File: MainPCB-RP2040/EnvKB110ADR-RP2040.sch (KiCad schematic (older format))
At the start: 272 parts, among them J2 EVQPU, J5 Conn_01x03_Male, U1 TLV75533PDBVR, U3 RP2040, Y1 3225_4P

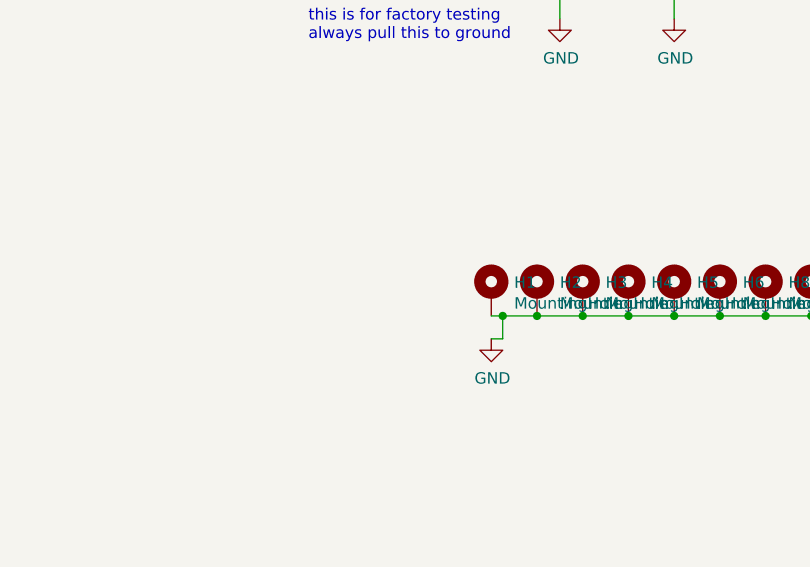
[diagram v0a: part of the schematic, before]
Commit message: added mount holes, fixed a couple trace errors, created backplate PCB
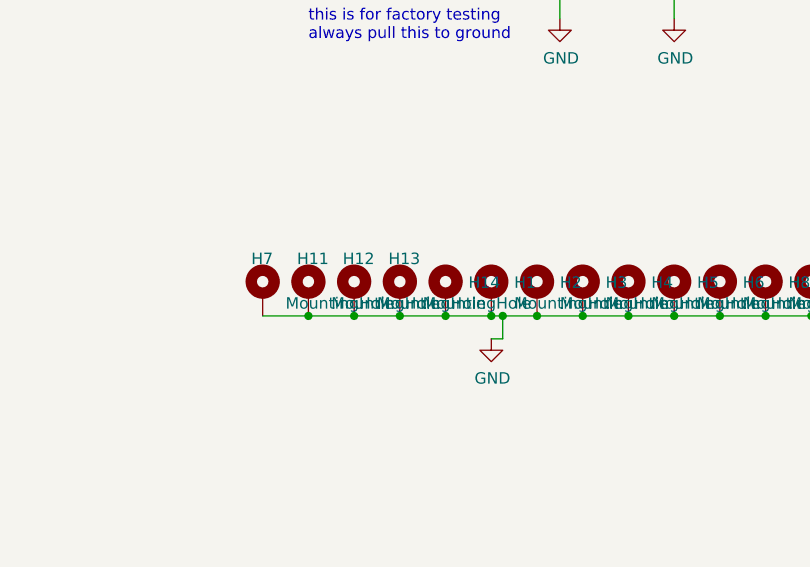
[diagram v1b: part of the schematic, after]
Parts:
- added H11, H12, H13, H14, H7: MountingHole, MountingHole:MountingHole_2.2mm_M2_Pad, symbol Mechanical:MountingHole_Pad
- H1, H10, H2, H3, H4, H5, H6, H8, H9: footprint MountingHole:MountingHole_2.2mm_M2 -> MountingHole:MountingHole_2.2mm_M2_Pad
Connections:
- net GND: now also H11.1, H12.1, H13.1, H14.1, H7.1
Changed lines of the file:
@@
 F 0 "H1" H 7100 9046 50  0000 L CNN
 F 1 "MountingHole" H 7100 8955 50  0000 L CNN
-F 2 "MountingHole:MountingHole_2.2mm_M2" H 7000 9000 50  0001 C CNN
+F 2 "MountingHole:MountingHole_2.2mm_M2_Pad" H 7000 9000 50  0001 C CNN
 F 3 "~" H 7000 9000 50  0001 C CNN
 	1    7000 9000
@@
 F 0 "H2" H 7300 9046 50  0000 L CNN
 F 1 "MountingHole" H 7300 8955 50  0000 L CNN
-F 2 "MountingHole:MountingHole_2.2mm_M2" H 7200 9000 50  0001 C CNN
+F 2 "MountingHole:MountingHole_2.2mm_M2_Pad" H 7200 9000 50  0001 C CNN
 F 3 "~" H 7200 9000 50  0001 C CNN
 	1    7200 9000
@@
 F 0 "H3" H 7500 9046 50  0000 L CNN
 F 1 "MountingHole" H 7500 8955 50  0000 L CNN
-F 2 "MountingHole:MountingHole_2.2mm_M2" H 7400 9000 50  0001 C CNN
+F 2 "MountingHole:MountingHole_2.2mm_M2_Pad" H 7400 9000 50  0001 C CNN
 F 3 "~" H 7400 9000 50  0001 C CNN
 	1    7400 9000
@@
 F 0 "H4" H 7700 9046 50  0000 L CNN
 F 1 "MountingHole" H 7700 8955 50  0000 L CNN
-F 2 "MountingHole:MountingHole_2.2mm_M2" H 7600 9000 50  0001 C CNN
+F 2 "MountingHole:MountingHole_2.2mm_M2_Pad" H 7600 9000 50  0001 C CNN
 F 3 "~" H 7600 9000 50  0001 C CNN
 	1    7600 9000
@@
 F 0 "H5" H 7900 9046 50  0000 L CNN
 F 1 "MountingHole" H 7900 8955 50  0000 L CNN
-F 2 "MountingHole:MountingHole_2.2mm_M2" H 7800 9000 50  0001 C CNN
+F 2 "MountingHole:MountingHole_2.2mm_M2_Pad" H 7800 9000 50  0001 C CNN
 F 3 "~" H 7800 9000 50  0001 C CNN
 	1    7800 9000
@@
 F 0 "H6" H 8100 9046 50  0000 L CNN
 F 1 "MountingHole" H 8100 8955 50  0000 L CNN
-F 2 "MountingHole:MountingHole_2.2mm_M2" H 8000 9000 50  0001 C CNN
+F 2 "MountingHole:MountingHole_2.2mm_M2_Pad" H 8000 9000 50  0001 C CNN
 F 3 "~" H 8000 9000 50  0001 C CNN
 	1    8000 9000
@@
 F 0 "H8" H 8300 9046 50  0000 L CNN
 F 1 "MountingHole" H 8300 8955 50  0000 L CNN
-F 2 "MountingHole:MountingHole_2.2mm_M2" H 8200 9000 50  0001 C CNN
+F 2 "MountingHole:MountingHole_2.2mm_M2_Pad" H 8200 9000 50  0001 C CNN
 F 3 "~" H 8200 9000 50  0001 C CNN
 	1    8200 9000
@@
 F 0 "H9" H 8500 9050 50  0000 L CNN
 F 1 "MountingHole" H 8500 8955 50  0000 L CNN
-F 2 "MountingHole:MountingHole_2.2mm_M2" H 8400 9000 50  0001 C CNN
+F 2 "MountingHole:MountingHole_2.2mm_M2_Pad" H 8400 9000 50  0001 C CNN
 F 3 "~" H 8400 9000 50  0001 C CNN
 	1    8400 9000
@@
 F 0 "H10" H 8700 9046 50  0000 L CNN
 F 1 "MountingHole" H 8700 8955 50  0000 L CNN
-F 2 "MountingHole:MountingHole_2.2mm_M2" H 8600 9000 50  0001 C CNN
+F 2 "MountingHole:MountingHole_2.2mm_M2_Pad" H 8600 9000 50  0001 C CNN
 F 3 "~" H 8600 9000 50  0001 C CNN
 	1    8600 9000
@@
 	1    0    0    -1
 $EndComp
+$Comp
+L Mechanical:MountingHole_Pad H14
+U 1 1 615CF2B5
+P 6800 9000
+F 0 "H14" H 6900 9046 50  0000 L CNN
+F 1 "MountingHole" H 6900 8955 50  0001 L CNN
+F 2 "MountingHole:MountingHole_2.2mm_M2_Pad" H 6800 9000 50  0001 C CNN
+F 3 "~" H 6800 9000 50  0001 C CNN
+	1    6800 9000
+	1    0    0    -1
+$EndComp
+$Comp
+L Mechanical:MountingHole_Pad H13
+U 1 1 615CF69F
+P 6600 9000
+F 0 "H13" H 6550 9150 50  0000 L CNN
+F 1 "MountingHole" H 6700 8955 50  0000 L CNN
+F 2 "MountingHole:MountingHole_2.2mm_M2_Pad" H 6600 9000 50  0001 C CNN
+F 3 "~" H 6600 9000 50  0001 C CNN
+	1    6600 9000
+	1    0    0    -1
+$EndComp
+$Comp
+L Mechanical:MountingHole_Pad H12
+U 1 1 615D178A
+P 6400 9000
+F 0 "H12" H 6350 9150 50  0000 L CNN
+F 1 "MountingHole" H 6500 8955 50  0000 L CNN
+F 2 "MountingHole:MountingHole_2.2mm_M2_Pad" H 6400 9000 50  0001 C CNN
+F 3 "~" H 6400 9000 50  0001 C CNN
+	1    6400 9000
+	1    0    0    -1
+$EndComp
+$Comp
+L Mechanical:MountingHole_Pad H11
+U 1 1 615D1AA3
+P 6200 9000
+F 0 "H11" H 6150 9150 50  0000 L CNN
+F 1 "MountingHole" H 6300 8955 50  0000 L CNN
+F 2 "MountingHole:MountingHole_2.2mm_M2_Pad" H 6200 9000 50  0001 C CNN
+F 3 "~" H 6200 9000 50  0001 C CNN
+	1    6200 9000
+	1    0    0    -1
+$EndComp
+Connection ~ 6400 9100
+Wire Wire Line
+	6400 9100 6200 9100
+Connection ~ 6600 9100
+Wire Wire Line
+	6600 9100 6400 9100
+Connection ~ 6800 9100
+Wire Wire Line
+	6800 9100 6600 9100
+Connection ~ 7000 9100
+Wire Wire Line
+	7000 9100 6800 9100
+$Comp
+L Mechanical:MountingHole_Pad H7
+U 1 1 61647CC2
+P 6000 9000
+F 0 "H7" H 5950 9150 50  0000 L CNN
+F 1 "MountingHole" H 6100 8955 50  0000 L CNN
+F 2 "MountingHole:MountingHole_2.2mm_M2_Pad" H 6000 9000 50  0001 C CNN
+F 3 "~" H 6000 9000 50  0001 C CNN
+	1    6000 9000
+	1    0    0    -1
+$EndComp
+Wire Wire Line
+	6000 9100 6200 9100
+Connection ~ 6200 9100
 $EndSCHEMATC

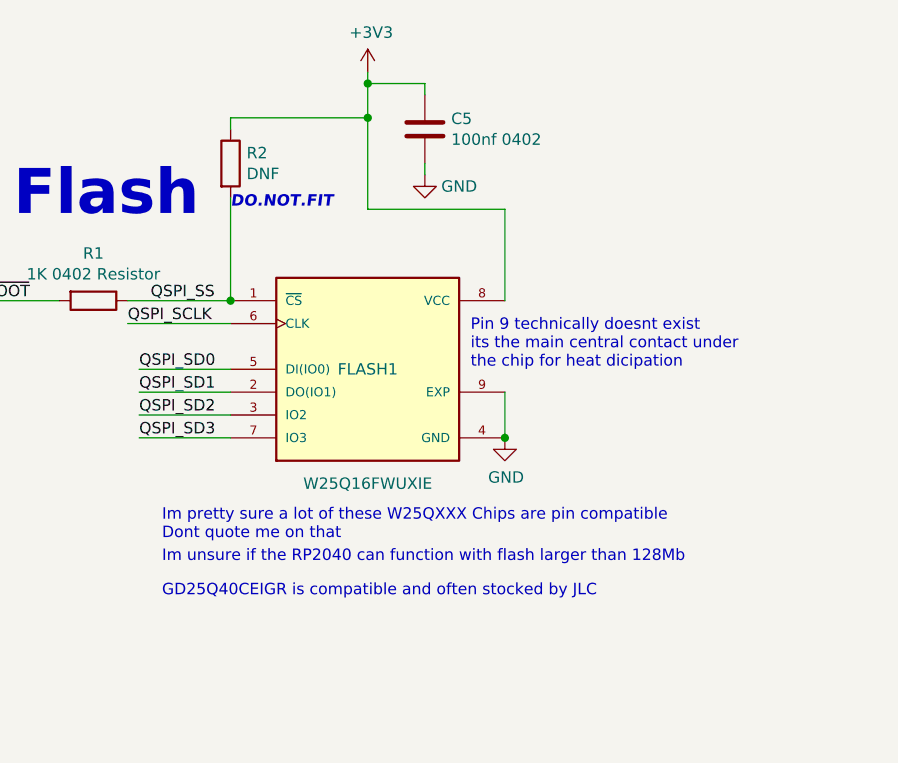
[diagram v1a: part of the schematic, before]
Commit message: corrections to design, via in pad and such
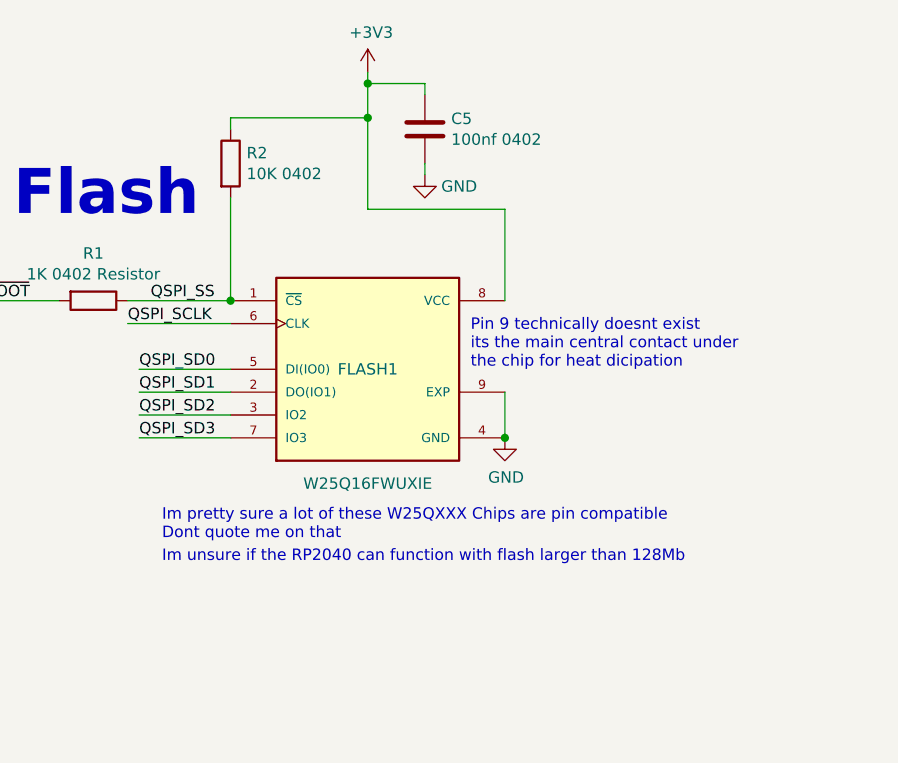
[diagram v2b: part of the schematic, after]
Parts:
- R2: value DNF -> 10K 0402
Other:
- note removed: "DO.NOT.FIT"
- note removed: "GD25Q40CEIGR is compatible and often stocked by JLC"
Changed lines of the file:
@@
 P 2500 4350
 F 0 "R2" H 2570 4396 50  0000 L CNN
-F 1 "DNF" H 2570 4305 50  0000 L CNN
+F 1 "10K 0402" H 2570 4305 50  0000 L CNN
 F 2 "Capacitor_SMD:C_0402_1005Metric" V 2430 4350 50  0001 C CNN
 F 3 "" H 2500 4350 50  0001 C CNN
@@
 Text Notes 4450 2700 0    50   Italic 0
 Only fit cBP1 if you have selected an \nalternate voltage regulator\n\nTLV75533PDBVR does not.
-Text Notes 2500 4550 0    50   Italic 10
-DO.NOT.FIT
-Text Notes 2200 6250 0    50   ~ 0
-GD25Q40CEIGR is compatible and often stocked by JLC
 $Comp
 L Device:R R11

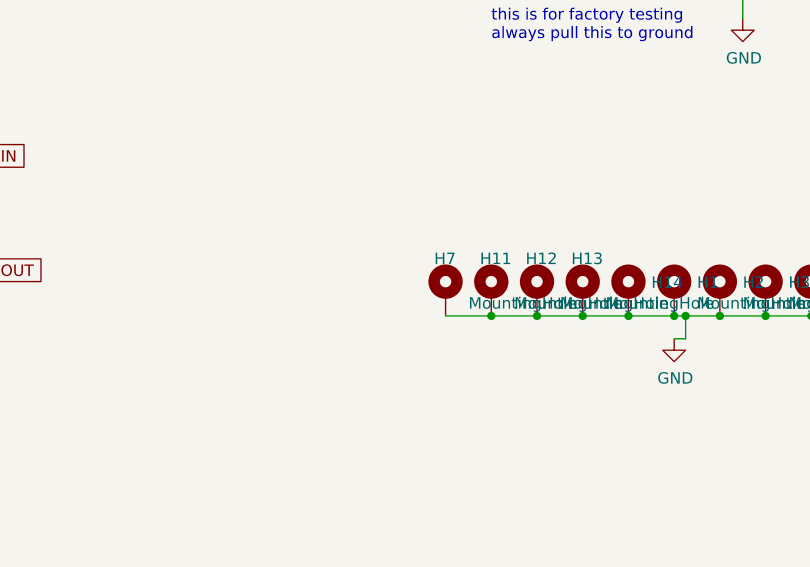
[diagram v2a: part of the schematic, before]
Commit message: added logo for black cat plastic works, couple urls and some fixes to design
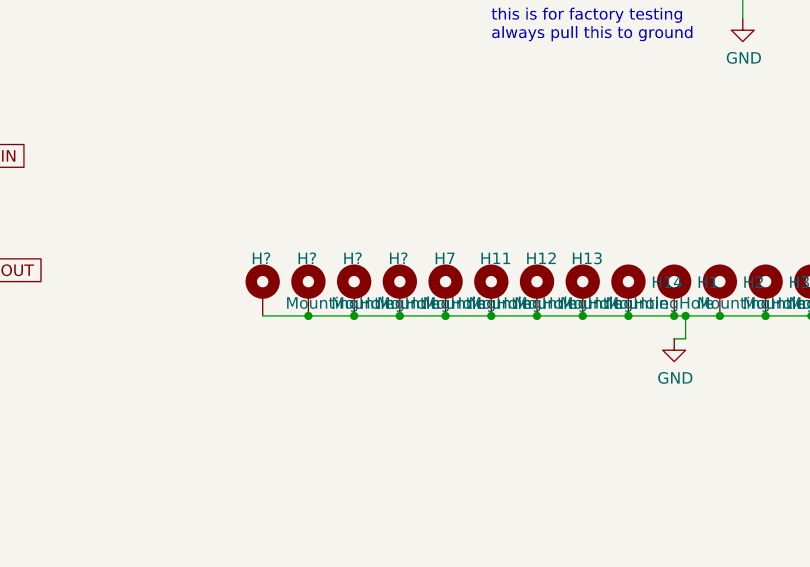
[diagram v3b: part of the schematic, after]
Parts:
- added H? (x4): MountingHole, MountingHole:MountingHole_2.2mm_M2_Pad, symbol Mechanical:MountingHole_Pad
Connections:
- net GND: now also H?.1, H?.1, H?.1, H?.1
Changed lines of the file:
@@
+	1    0    0    -1
+$EndComp
+Connection ~ 6200 9100
+$Comp
+L Mechanical:MountingHole_Pad H?
+U 1 1 61A6E8C5
+P 5800 9000
+F 0 "H?" H 5750 9150 50  0000 L CNN
+F 1 "MountingHole" H 5900 8955 50  0000 L CNN
+F 2 "MountingHole:MountingHole_2.2mm_M2_Pad" H 5800 9000 50  0001 C CNN
+F 3 "~" H 5800 9000 50  0001 C CNN
+	1    5800 9000
+	1    0    0    -1
+$EndComp
+$Comp
+L Mechanical:MountingHole_Pad H?
+U 1 1 61A6EE1C
+P 5600 9000
+F 0 "H?" H 5550 9150 50  0000 L CNN
+F 1 "MountingHole" H 5700 8955 50  0000 L CNN
+F 2 "MountingHole:MountingHole_2.2mm_M2_Pad" H 5600 9000 50  0001 C CNN
+F 3 "~" H 5600 9000 50  0001 C CNN
+	1    5600 9000
+	1    0    0    -1
+$EndComp
+$Comp
+L Mechanical:MountingHole_Pad H?
+U 1 1 61A6F3C0
+P 5400 9000
+F 0 "H?" H 5350 9150 50  0000 L CNN
+F 1 "MountingHole" H 5500 8955 50  0000 L CNN
+F 2 "MountingHole:MountingHole_2.2mm_M2_Pad" H 5400 9000 50  0001 C CNN
+F 3 "~" H 5400 9000 50  0001 C CNN
+	1    5400 9000
+	1    0    0    -1
+$EndComp
+$Comp
+L Mechanical:MountingHole_Pad H?
+U 1 1 61A73E9B
+P 5200 9000
+F 0 "H?" H 5150 9150 50  0000 L CNN
+F 1 "MountingHole" H 5300 8955 50  0000 L CNN
+F 2 "MountingHole:MountingHole_2.2mm_M2_Pad" H 5200 9000 50  0001 C CNN
+F 3 "~" H 5200 9000 50  0001 C CNN
+	1    5200 9000
 	1    0    0    -1
 $EndComp
 Wire Wire Line
+	5200 9100 5400 9100
+Connection ~ 5400 9100
+Wire Wire Line
+	5400 9100 5600 9100
+Connection ~ 5600 9100
+Wire Wire Line
+	5600 9100 5800 9100
+Connection ~ 5800 9100
+Wire Wire Line
+	5800 9100 6000 9100
+Connection ~ 6000 9100
+Wire Wire Line
 	6000 9100 6200 9100
-Connection ~ 6200 9100
 $EndSCHEMATC

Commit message: Update EnvKB110ADR-RP2040.sch
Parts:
- gave numbers to parts that had none: 4
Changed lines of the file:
@@
 Connection ~ 6200 9100
 $Comp
-L Mechanical:MountingHole_Pad H?
+L Mechanical:MountingHole_Pad H18
 U 1 1 61A6E8C5
 P 5800 9000
-F 0 "H?" H 5750 9150 50  0000 L CNN
+F 0 "H18" H 5750 9150 50  0000 L CNN
 F 1 "MountingHole" H 5900 8955 50  0000 L CNN
 F 2 "MountingHole:MountingHole_2.2mm_M2_Pad" H 5800 9000 50  0001 C CNN
@@
 $EndComp
 $Comp
-L Mechanical:MountingHole_Pad H?
+L Mechanical:MountingHole_Pad H17
 U 1 1 61A6EE1C
 P 5600 9000
-F 0 "H?" H 5550 9150 50  0000 L CNN
+F 0 "H17" H 5550 9150 50  0000 L CNN
 F 1 "MountingHole" H 5700 8955 50  0000 L CNN
 F 2 "MountingHole:MountingHole_2.2mm_M2_Pad" H 5600 9000 50  0001 C CNN
@@
 $EndComp
 $Comp
-L Mechanical:MountingHole_Pad H?
+L Mechanical:MountingHole_Pad H16
 U 1 1 61A6F3C0
 P 5400 9000
-F 0 "H?" H 5350 9150 50  0000 L CNN
+F 0 "H16" H 5350 9150 50  0000 L CNN
 F 1 "MountingHole" H 5500 8955 50  0000 L CNN
 F 2 "MountingHole:MountingHole_2.2mm_M2_Pad" H 5400 9000 50  0001 C CNN
@@
 $EndComp
 $Comp
-L Mechanical:MountingHole_Pad H?
+L Mechanical:MountingHole_Pad H15
 U 1 1 61A73E9B
 P 5200 9000
-F 0 "H?" H 5150 9150 50  0000 L CNN
+F 0 "H15" H 5150 9150 50  0000 L CNN
 F 1 "MountingHole" H 5300 8955 50  0000 L CNN
 F 2 "MountingHole:MountingHole_2.2mm_M2_Pad" H 5200 9000 50  0001 C CNN

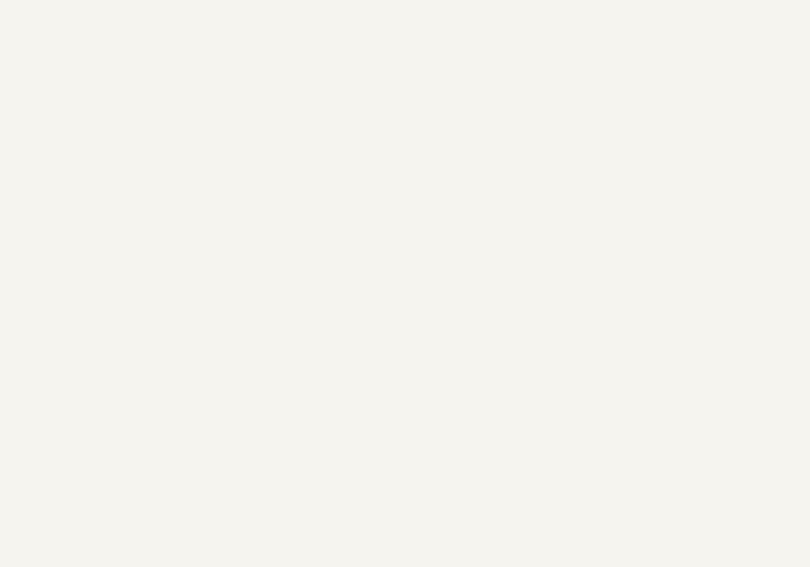
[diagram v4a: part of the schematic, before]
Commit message: replaced switch footprints with stronger versions and SMT assembly compatible versions
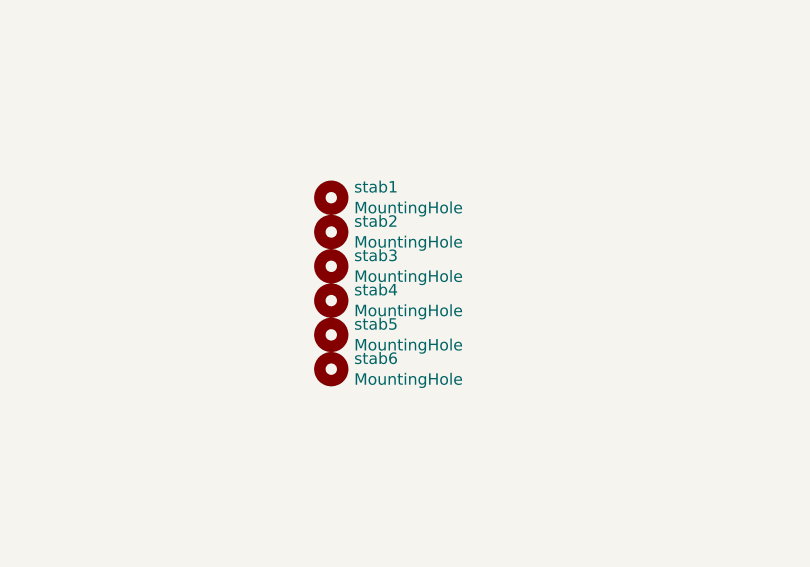
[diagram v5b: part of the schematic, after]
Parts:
- added stab1, stab2, stab3, stab4, stab6: MountingHole, Mounting_Keyboard_Stabilizer:Stabilizer_Cherry_MX_2u, symbol Mechanical:MountingHole
- added stab5: MountingHole, Mounting_Keyboard_Stabilizer:Stabilizer_Cherry_MX_6.25u, symbol Mechanical:MountingHole
- K_100, K_101, K_102, K_112, K_113, K_114, K_116, K_12, K_13, K_14, K_15, K_16, K_17, K_18, K_19, K_20, K_21, K_22, K_23, K_24, K_25, K_26, K_27, K_28, K_29, K_30, K_31, K_32, K_33, K_34, K_35, K_36, K_37, K_38, K_39, K_40, K_42, K_43, K_44, K_45, K_46, K_47, K_48, K_50, K_51, K_52, K_53, K_54, K_55, K_56, K_57, K_58, K_59, K_60, K_61, K_63, K_64, K_65, K_66, K_67, K_68, K_71, K_72, K_73, K_74, K_75, K_76, K_77, K_78, K_79, K_80, K_81, K_82, K_83, K_84, K_85, K_87, K_88, K_89, K_90, K_91, K_92, K_93, K_94, K_95, K_96, K_97, K_99: footprint MX_Only:MXOnly-1U-Hotswap -> MX_Only:MXOnly-1U-Hotswap-custom
- K_103, K_115, K_41, K_62, K_69: footprint MX_Only:MXOnly-2U-Hotswap -> MX_Only:MXOnly-1U-Hotswap-custom
- K_104, K_105, K_106, K_108, K_109, K_110, K_111, K_86: footprint MX_Only:MXOnly-1.25U-Hotswap -> MX_Only:MXOnly-1U-Hotswap-custom
- K_107: footprint MX_Only:MXOnly-6.25U-Hotswap-ReversedStabilizers -> MX_Only:MXOnly-1U-Hotswap-custom
- K_49, K_ANSI_3: footprint MX_Only:MXOnly-1.5U-Hotswap -> MX_Only:MXOnly-1U-Hotswap-custom
- K_70: footprint MX_Only:MXOnly-1.75U-Hotswap -> MX_Only:MXOnly-1U-Hotswap-custom
- K_98: footprint MX_Only:MXOnly-2.75U-Hotswap -> MX_Only:MXOnly-1U-Hotswap-custom
- K_ANSI_1, K_ANSI_2: footprint MX_Only:MXOnly-2.25U-Hotswap -> MX_Only:MXOnly-1U-Hotswap-custom
